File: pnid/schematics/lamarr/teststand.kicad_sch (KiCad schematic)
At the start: 55 parts

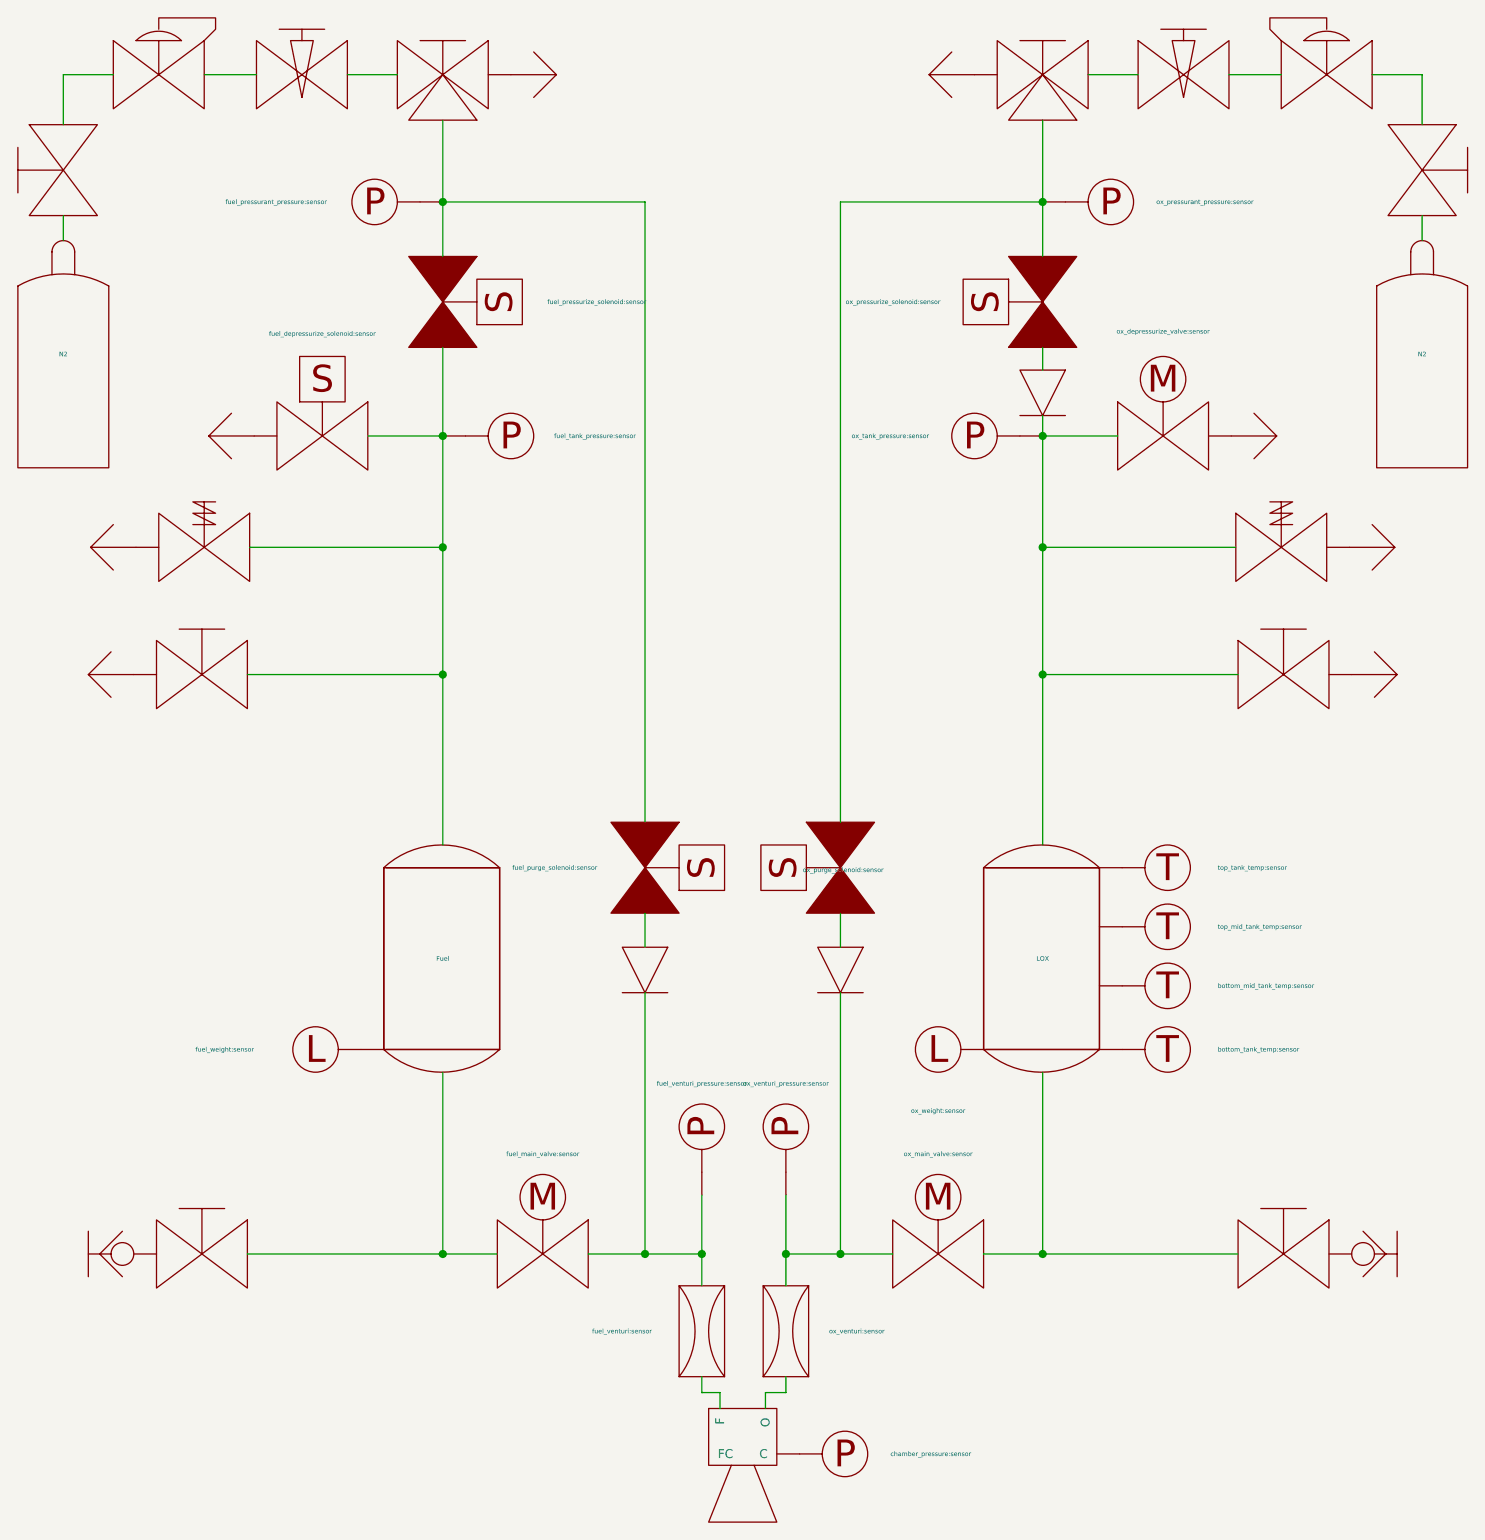
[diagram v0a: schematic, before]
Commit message: improve label placement for remaining pnids
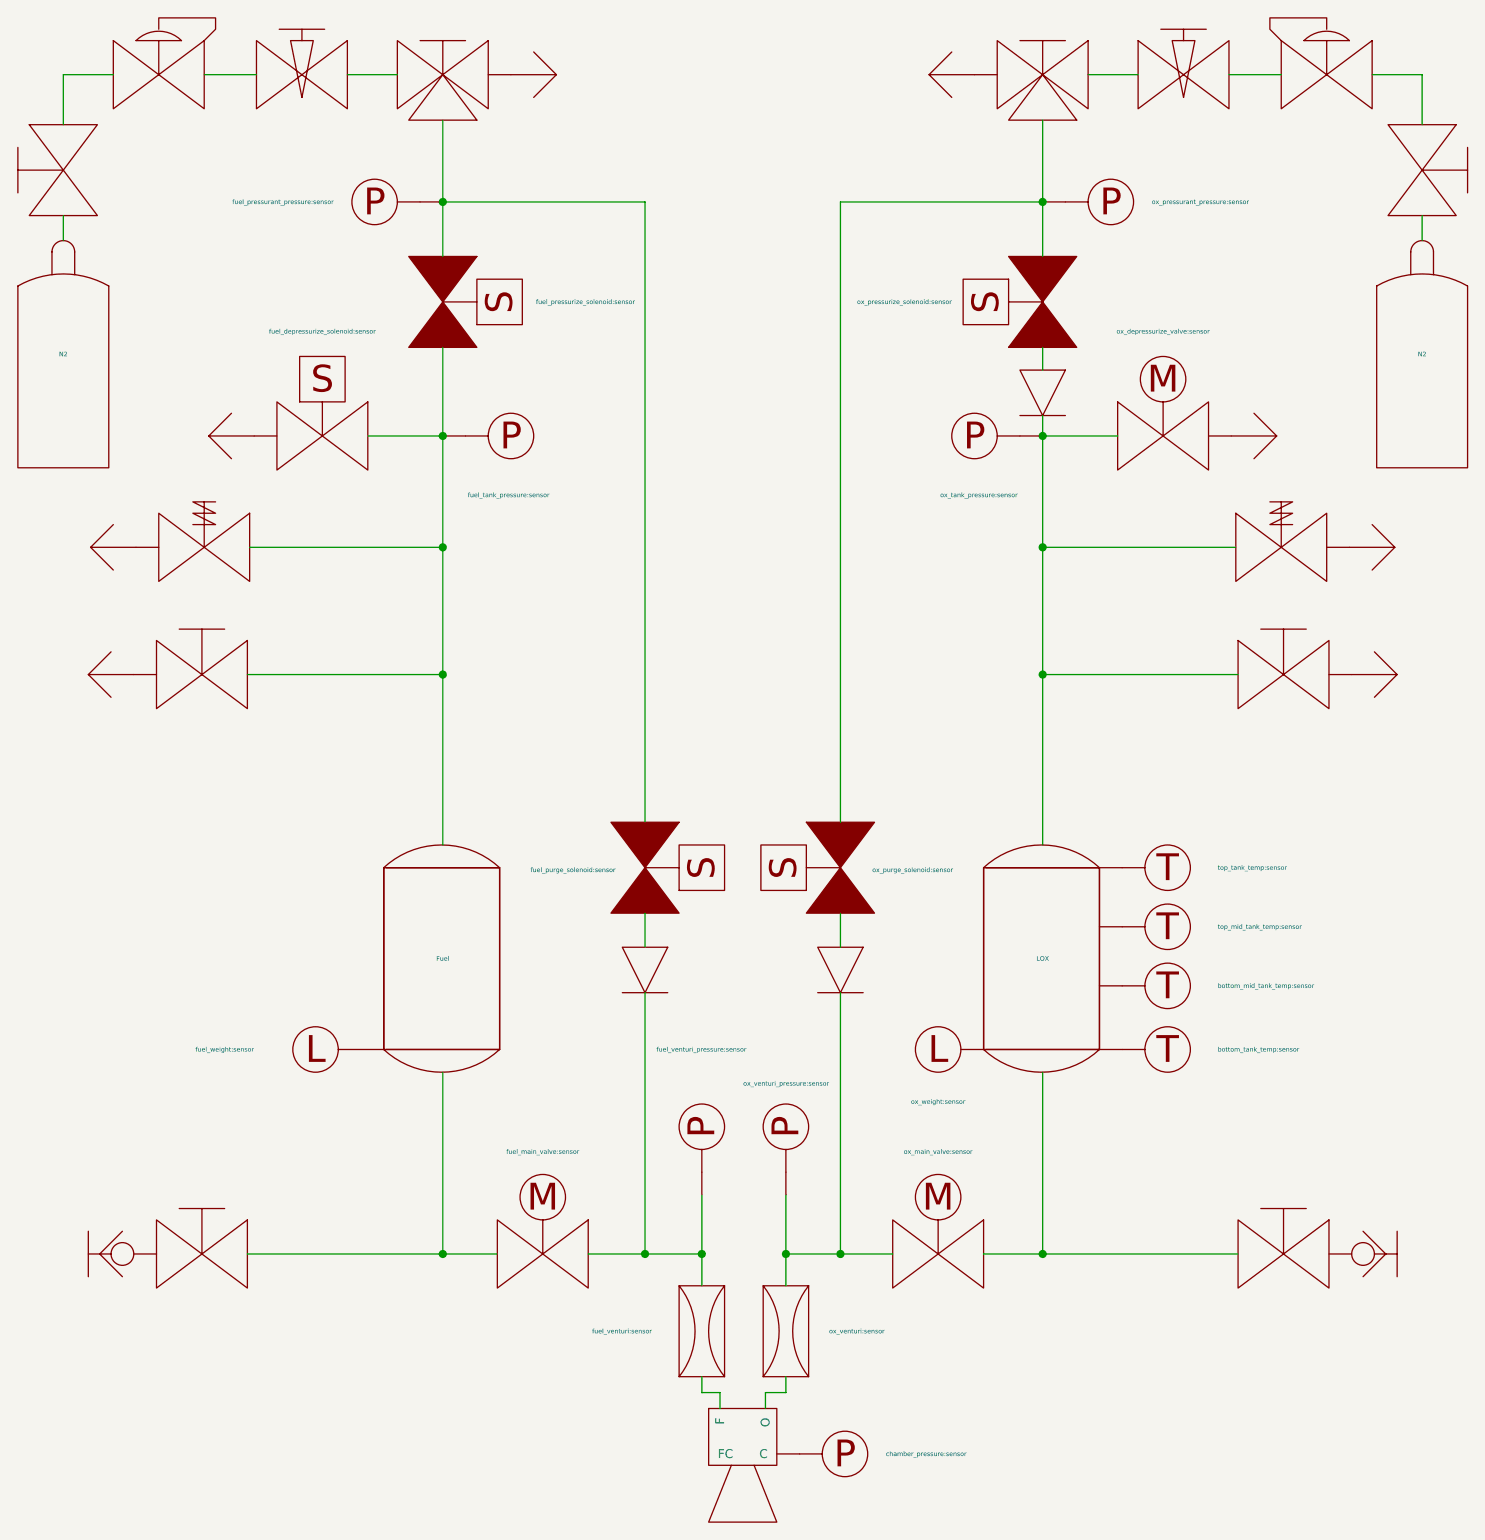
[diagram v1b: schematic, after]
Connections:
- net at engine.~ (O): now also fuel_venturi.~
- net at ox_venturi.~: now also CheckValve?.~, ox_main_valve.~, ox_venturi_pressure.~; no longer engine.~ (O)
- net at fuel_venturi.~: now also CheckValve?.~, fuel_main_valve.~, fuel_venturi_pressure.~; no longer engine.~ (O)
- net at ox_pressure_regulator.~: now also ox_manual_valve.~; no longer ox_needle_valve.~
- net at ox_manual_valve.~: now also N2.~; no longer ox_pressure_regulator.~
- new net: fuel_manual_3way?.~, ox_pressurant_pressure:sensor.~, ox_pressurize_solenoid.~, ox_purge_solenoid.~
- new net: fuel_manual_3way.~, fuel_pressurant_pressure.~, fuel_pressurize_solenoid.~, fuel_purge_solenoid.~
- new net: Fuel.~, fuel_depressurize_solenoid.~, fuel_manual_vent_valve.~, fuel_pressurize_solenoid.~, fuel_safety_valve.~, fuel_tank_pressure.~
- new net: CheckValve?.~, LOX.~, ox_depressurize_valve.~, ox_manual_vent_valve.~, ox_safety_valve.~, ox_tank_pressure.~
- new net: LOX.~, ox_main_valve.~, ox_manual_tanking_valve.~
- new net: Fuel.~, fuel_main_valve.~, fuel_manual_tanking_valve.~
- new net: engine.~ (O), ox_venturi.~
- new net: ox_needle_valve.~, ox_pressure_regulator.~
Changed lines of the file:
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@@
 		)
 		(property "Value" "ox_pressurant_pressure:sensor"
-			(at 145.542 37.084 0)
+			(at 145.034 37.084 0)
 			(effects
 				(font
@@
 		)
 		(property "Value" "fuel_pressurant_pressure:sensor"
-			(at 52.832 37.084 0)
+			(at 53.594 37.084 0)
 			(effects
 				(font
@@
 		)
 		(property "Value" "ox_pressurize_solenoid:sensor"
-			(at 121.412 48.26 90)
+			(at 122.682 48.26 90)
 			(effects
 				(font
@@
 		)
 		(property "Value" "fuel_pressurize_solenoid:sensor"
-			(at 77.47 48.26 90)
+			(at 76.2 48.26 90)
 			(effects
 				(font
@@
 		)
 		(property "Value" "ox_purge_solenoid:sensor"
-			(at 115.062 111.76 90)
+			(at 113.792 111.76 90)
 			(effects
 				(font
 					(size 0.508 0.508)
 				)
-				(justify left)
+				(justify right)
 			)
 		)
@@
 		)
 		(property "Value" "fuel_purge_solenoid:sensor"
-			(at 83.058 111.506 90)
+			(at 85.09 111.76 90)
 			(effects
 				(font
@@
 	)
 	(symbol
-		(lib_name "PnID-Lib:CheckValve")
 		(lib_id "PnID-Lib:CheckValve")
 		(at 132.842 58.42 270)
@@
 	)
 	(symbol
-		(lib_name "PnID-Lib:Tank_Slim")
 		(lib_id "PnID-Lib:Tank_Slim")
 		(at 132.842 121.666 0)
@@
 	)
 	(symbol
-		(lib_name "PnID-Lib:Tank_Slim")
 		(lib_id "PnID-Lib:Tank_Slim")
 		(at 65.786 121.666 0)
@@
 	)
 	(symbol
-		(lib_name "PnID-Lib:Engine")
 		(lib_id "PnID-Lib:Engine")
 		(at 99.314 174.498 0)
@@
 	)
 	(symbol
-		(lib_name "PnID-Lib:CheckValve")
 		(lib_id "PnID-Lib:CheckValve")
 		(at 88.392 122.936 270)
@@
 	)
 	(symbol
-		(lib_name "PnID-Lib:CheckValve")
 		(lib_id "PnID-Lib:CheckValve")
 		(at 110.236 122.936 270)
@@
 		)
 		(property "Value" "fuel_venturi_pressure:sensor"
-			(at 94.742 135.636 90)
+			(at 89.662 131.826 90)
 			(effects
 				(font
 					(size 0.508 0.508)
 				)
+				(justify right)
 			)
 		)
@@
 		)
 		(property "Value" "ox_venturi_pressure:sensor"
-			(at 104.14 135.636 90)
+			(at 108.966 135.636 90)
 			(effects
 				(font
 					(size 0.508 0.508)
 				)
+				(justify left)
 			)
 		)
@@
 		)
 		(property "Value" "chamber_pressure:sensor"
-			(at 115.824 177.038 0)
+			(at 115.316 177.038 0)
 			(effects
 				(font
@@
 	)
 	(symbol
-		(lib_name "PnID-Lib:Valve_Manual")
 		(lib_id "PnID-Lib:Valve_Manual")
 		(at 159.766 154.686 0)
@@
 	)
 	(symbol
-		(lib_name "PnID-Lib:Venturi")
 		(lib_id "PnID-Lib:Venturi")
 		(at 104.14 163.322 270)
@@
 	)
 	(symbol
-		(lib_name "PnID-Lib:Venturi")
 		(lib_id "PnID-Lib:Venturi")
 		(at 94.742 163.322 270)
@@
 	)
 	(symbol
-		(lib_name "PnID-Lib:Valve_Manual")
 		(lib_id "PnID-Lib:Valve_Manual")
 		(at 23.368 33.528 90)
@@
 	)
 	(symbol
-		(lib_name "PnID-Lib:PressureRegulator")
 		(lib_id "PnID-Lib:PressureRegulator")
 		(at 34.036 22.86 0)
@@
 	)
 	(symbol
-		(lib_name "PnID-Lib:Valve_Needle")
 		(lib_id "PnID-Lib:Valve_Needle")
 		(at 50.038 22.86 0)
@@
 	)
 	(symbol
-		(lib_name "teststand-rescue:Valve_Manual_3Way-PnID-Lib")
 		(lib_id "teststand-rescue:Valve_Manual_3Way-PnID-Lib")
 		(at 65.786 29.972 0)
@@
 	)
 	(symbol
-		(lib_name "PnID-Lib:Valve_OverPressure")
 		(lib_id "PnID-Lib:Valve_OverPressure")
 		(at 39.116 75.692 0)
@@
 	)
 	(symbol
-		(lib_name "PnID-Lib:Valve_Solenoid_NO")
 		(lib_id "PnID-Lib:Valve_Solenoid_NO")
 		(at 52.324 63.246 0)
@@
 		)
 		(property "Value" "fuel_depressurize_solenoid:sensor"
-			(at 52.324 51.816 0)
+			(at 52.324 51.562 0)
 			(effects
 				(font
@@
 	)
 	(symbol
-		(lib_name "PnID-Lib:Valve_Manual")
 		(lib_id "PnID-Lib:Valve_Manual")
 		(at 38.862 154.686 0)
@@
 	)
 	(symbol
-		(lib_name "PnID-Lib:Valve_Manual")
 		(lib_id "PnID-Lib:Valve_Manual")
 		(at 38.862 89.916 0)
@@
 		)
 		(property "Value" "fuel_main_valve:sensor"
-			(at 76.962 143.51 0)
+			(at 76.962 143.256 0)
 			(effects
 				(font
@@
 	)
 	(symbol
-		(lib_name "PnID-Lib:Valve_OverPressure")
 		(lib_id "PnID-Lib:Valve_OverPressure")
 		(at 159.512 75.692 0)
@@
 	)
 	(symbol
-		(lib_name "PnID-Lib:Valve_Servo")
 		(lib_id "PnID-Lib:Valve_Servo")
 		(at 146.304 63.246 0)
@@
 	)
 	(symbol
-		(lib_name "PnID-Lib:Valve_Manual")
 		(lib_id "PnID-Lib:Valve_Manual")
 		(at 159.766 89.916 0)
@@
 		)
 		(property "Value" "fuel_tank_pressure:sensor"
-			(at 78.232 63.246 0)
+			(at 68.58 69.85 0)
 			(effects
 				(font
@@
 		)
 		(property "Value" "ox_tank_pressure:sensor"
-			(at 120.142 63.246 0)
+			(at 130.048 69.85 0)
 			(effects
 				(font
@@
 	)
 	(symbol
-		(lib_name "PnID-Lib:PressureRegulator")
 		(lib_id "PnID-Lib:PressureRegulator")
 		(at 164.592 22.86 0)
@@
 	)
 	(symbol
-		(lib_name "PnID-Lib:Valve_Needle")
 		(lib_id "PnID-Lib:Valve_Needle")
 		(at 148.59 22.86 0)
@@
 	)
 	(symbol
-		(lib_name "PnID-Lib:Valve_Manual")
 		(lib_id "PnID-Lib:Valve_Manual")
 		(at 175.26 33.528 270)
@@
 	)
 	(symbol
-		(lib_name "teststand-rescue:Valve_Manual_3Way-PnID-Lib")
 		(lib_id "teststand-rescue:Valve_Manual_3Way-PnID-Lib")
 		(at 132.842 29.972 0)
@@
 		)
 		(property "Value" "ox_main_valve:sensor"
-			(at 121.158 143.51 0)
+			(at 121.158 143.256 0)
 			(effects
 				(font
@@
 		)
 		(property "Value" "ox_weight:sensor"
-			(at 121.158 138.684 0)
+			(at 121.158 137.668 0)
 			(effects
 				(font

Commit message: dump changes from hotfire prep
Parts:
- removed ox_manual_tanking_valve: ox_manual_tanking_valve, symbol PnID-Lib:Valve_Manual
- added U1: sound_supression:sensor, symbol PnID-Lib:Pump
- added heater1: tank_heating:sensor, symbol PnID-Lib:heater
- added ox_purge_solenoid1: safety_valves:sensor, symbol PnID-Lib:Valve_Solenoid_NC
- added tanking_valve1: tanking_valve:sensor, symbol PnID-Lib:Valve_Servo
- ox_depressurize_solenoid: renamed from ox_depressurize_valve; value ox_depressurize_valve:sensor -> ox_depressurize_solenoid:sensor; symbol PnID-Lib:Valve_Servo -> PnID-Lib:Valve_Solenoid_NO
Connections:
- net at LOX.~, ox_main_valve.~: now also tanking_valve1.~
- net at engine.~ (O): now also fuel_venturi.~
- net at ox_venturi.~: now also CheckValve?.~, ox_main_valve.~, ox_venturi_pressure.~; no longer engine.~ (O)
- net at fuel_venturi.~: now also CheckValve?.~, fuel_main_valve.~, fuel_venturi_pressure.~; no longer engine.~ (O)
- net at ox_quick_connect.~: now also tanking_valve1.~
- net at ox_pressure_regulator.~: now also ox_manual_valve.~; no longer ox_needle_valve.~
- net at ox_manual_valve.~: now also N2.~; no longer ox_pressure_regulator.~
- new net: fuel_manual_3way?.~, ox_pressurant_pressure:sensor.~, ox_pressurize_solenoid.~, ox_purge_solenoid.~
- new net: fuel_manual_3way.~, fuel_pressurant_pressure.~, fuel_pressurize_solenoid.~, fuel_purge_solenoid.~
- new net: Fuel.~, fuel_depressurize_solenoid.~, fuel_manual_vent_valve.~, fuel_pressurize_solenoid.~, fuel_safety_valve.~, fuel_tank_pressure.~
- new net: CheckValve?.~, LOX.~, ox_depressurize_solenoid.~, ox_manual_vent_valve.~, ox_safety_valve.~, ox_tank_pressure.~
- new net: Fuel.~, fuel_main_valve.~, fuel_manual_tanking_valve.~
- new net: engine.~ (O), ox_venturi.~
- new net: ox_needle_valve.~, ox_pressure_regulator.~
